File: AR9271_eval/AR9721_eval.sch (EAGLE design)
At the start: 125 parts, among them J1 UJ2-MIBH2-4-SMT-TR, J3 HTST-110-01-XX-DV, J7 132134-15, J8 132134-15, U1 U-ATHEROS-AR9271, U2 AT24C04C-XHM-T, U3 LT3080EQPBF, U4 LT3080EQPBF, U5 LT3080EQPBF, U6 LT3080EQPBF, Y1 ECS-400-10-36-CKY-TR

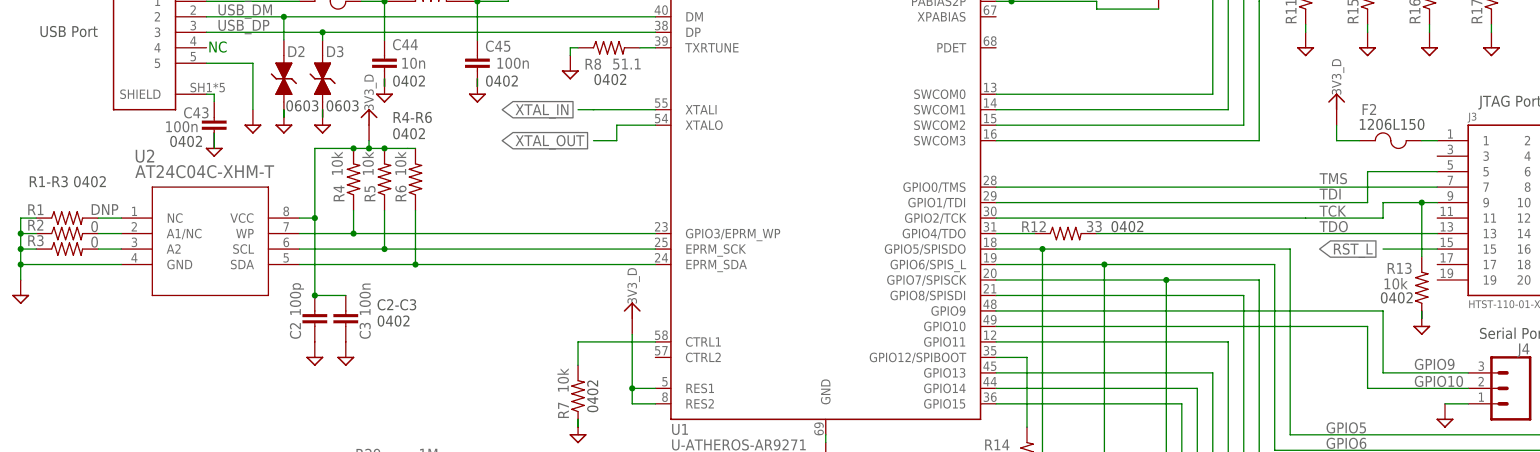
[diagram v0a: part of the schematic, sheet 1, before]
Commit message: BRD and SCH now back in sync
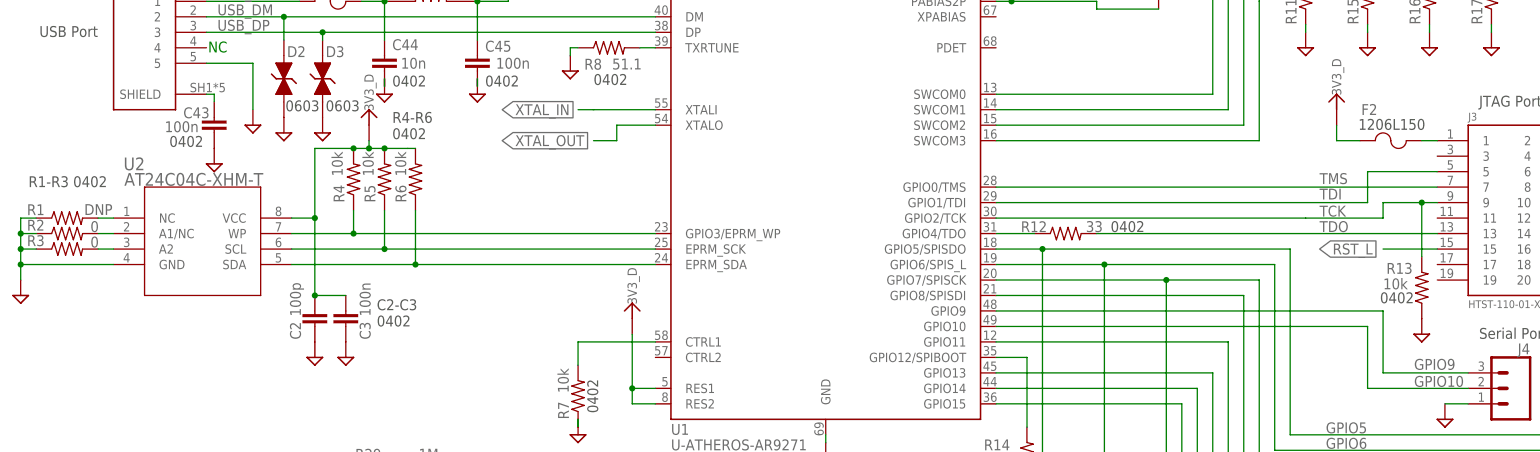
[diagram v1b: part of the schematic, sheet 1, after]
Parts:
- U2: device AT24C04_TSSOP:AT24C04C-XHM-T -> U-Generic-AT24C04-EEPROM-I2C-4Kb-TSSOP:AT24C04C-XHM-T; MPN AT24C04CXHMT -> (none)
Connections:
- removed net GND1: C43.2, D2.2, D3.2, J1.5, J2.1, J2.2, J2.7, J2.8, J3.10, J3.12, J3.14, J3.16, J3.18, J3.20, J3.4, J3.6, J3.8, J4.1, J5.1, J6.1, R1.1, R13.1, R14.1, R2.1, R3.1, U1.GND, U2.GND
- net GND: now also C43.2, D2.2, D3.2, J1.5, J2.1, J2.2, J2.7, J2.8, J3.10, J3.12, J3.14, J3.16, J3.18, J3.20, J3.4, J3.6, J3.8, J4.1, J5.1, J6.1, R1.1, R13.1, R14.1, R2.1, R3.1, U1.GND, U2.GND
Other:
- moved on the sheet: U2

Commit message: First pass of the updated AR9271 dev board. Took Stephen's fine board, and OCD'd it. Still requires stiching, better LAYER3 power layout, TNAMES cleanup, better stiching, but it's close!
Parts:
- removed F1, F2: 1206L150THWR, Polyfuse_1206L150:1206L150THWR
- removed J2: (no value), SparkFun-Connectors:CONN_08LONGPADS
- removed J4: (no value), SparkFun-Connectors:CONN_03LONGPADS
- removed J5: (no value), SparkFun-Connectors:CONN_05
- removed J6: (no value), SparkFun-Connectors:CONN_09LONGPADS
- added C52: 1u, oresat-rcl:C-EU0402-B-NOSILK
- added JP1: (no value), pinhead:PINHD-1X5
- added JP2: (no value), pinhead:PINHD-1X3
- added JP3: (no value), pinhead:PINHD-1X9
- added JP4: (no value), pinhead:PINHD-1X8
- added TP1, TP2, TP3, TP4, TP5: TPTP06R, testpad:TPTP06R
- C2: value 100p -> 100n; MPN GCM1555C1H101JA16D -> GRM155R70J105KA12J
- C35, C36: value 10.0pF -> 10p
- C37: value 100pF -> 100p
- C38, C40: value 1000pF -> 1n
- C39: value 10nF -> 10n
- C41, C42: value 1uF -> 1u
- R5, R6: value 10k -> 4.7k
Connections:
- net N$11 renamed BIASREF
- net N$16 renamed TDO-PRE-RES
- net N$2 renamed TXRTUNE
- net N$3 renamed EE-WP
- net N$4 renamed EE-SCK
- net N$5 renamed EE-SDA
- net N$8 renamed A1
- net N$9 renamed A2
- net RST_L renamed !RST
- net XTAL_IN renamed XTALI
- net XTAL_OUT renamed XTALO
- removed net N$1: R7.2, U1.CTRL1
- removed net N$10: R14.2, U1.GPIO12/SPIBOOT
- removed net N$31: C44.1, F1.2, L5.1
- removed net N$32: F2.2, J3.1
- new net CTRL1: R7.2, TP1.TP, U1.CTRL1
- new net CTRL2: TP2.TP, U1.CTRL2
- new net PDET: TP4.TP, U1.PDET
- new net SPIBOOT: R14.2, TP5.TP, U1.GPIO12/SPIBOOT
- new net XPABIOS: TP3.TP, U1.XPABIAS
- net 1V2_A: now also C2.1
- net 3V3_A: now also C52.1
- net 3V3_D: now also J3.1; no longer C2.1, F2.1
- net GND: now also C52.2, JP1.5, JP2.3, JP3.9, JP4.1, JP4.2, JP4.7, JP4.8; no longer J2.1, J2.2, J2.7, J2.8, J4.1, J5.1, J6.1
- net GPIO10: now also JP2.2; no longer J4.2
- net GPIO11: now also JP3.5; no longer J6.5
- net GPIO13: now also JP3.6; no longer J6.4
- net GPIO14: now also JP3.7; no longer J6.3
- net GPIO15: now also JP3.8; no longer J6.2
- net GPIO5: now also JP3.1; no longer J6.9
- net GPIO6: now also JP3.2; no longer J6.8
- net GPIO7: now also JP3.3; no longer J6.7
- net GPIO8: now also JP3.4; no longer J6.6
- net GPIO9: now also JP2.1; no longer J4.3
- net LDO_IN: now also JP4.5; no longer J2.4
- net N$6: now also JP4.3, JP4.4; no longer J2.5, J2.6
- net SWCOM0: now also JP1.1; no longer J5.5
- net SWCOM1: now also JP1.2; no longer J5.4
- net SWCOM2: now also JP1.3; no longer J5.3
- net SWCOM3: now also JP1.4; no longer J5.2
- net USB+5V: now also JP4.6; no longer J2.3
- net USB_+V: now also C44.1, L5.1; no longer F1.1
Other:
- note added: "40 MHz"
- note added: "DC Power Select"
- note added: "To RF feed"
- note added: "by 53"
- note added: "by p 56, 59,61"
- note removed: "0402"
- note removed: "1206L150"
- note removed: "All LEDs 0603 All dropping resistors 0402 All dropping resistors 510 Ohms for ~2.5mA LED current"
- note removed: "C2-C3 0402"
- note removed: "C4-C5 0402"
- note removed: "DC Power"
- note removed: "R1-R3 0402"
- note removed: "R4-R6 0402"
- note removed: "by p 59,61"
- moved on the sheet: C24, C25, C26, C27, C28, C29, C3, C30, C31, C32, C33, C34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

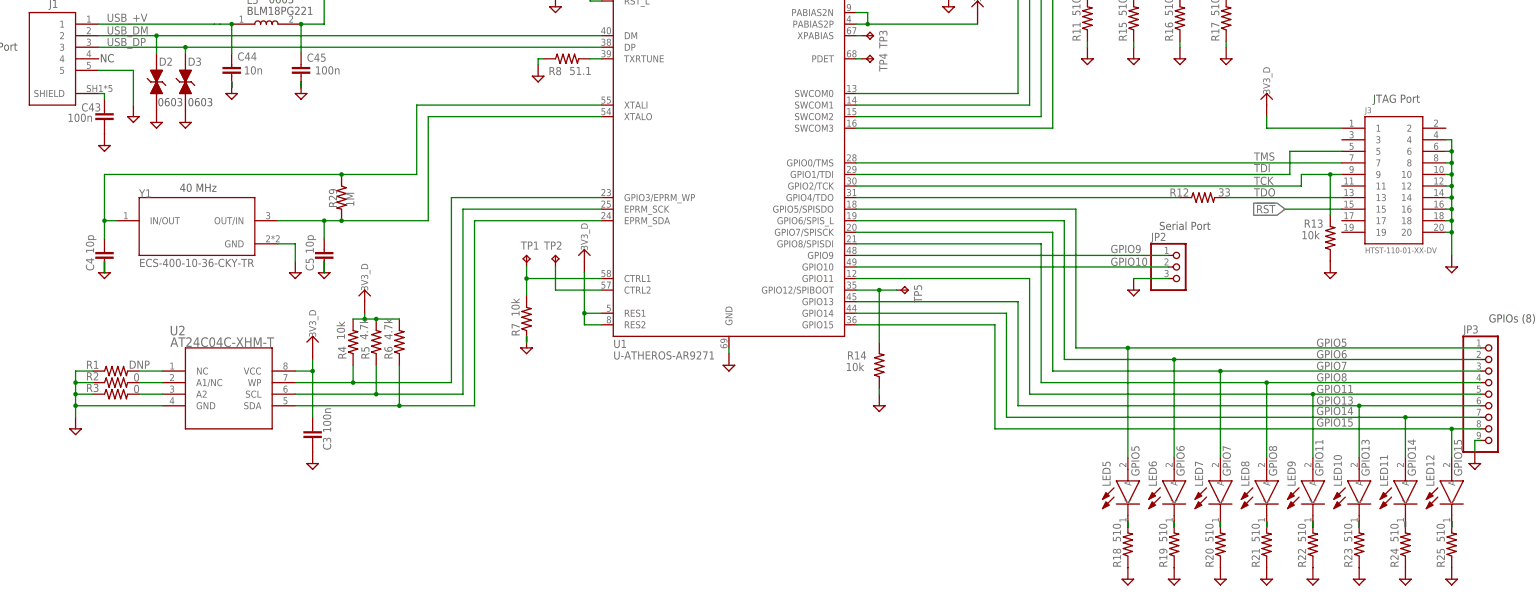
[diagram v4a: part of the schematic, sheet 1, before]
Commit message: More stitching, polishing of power layer, no ERCs or DRCs.
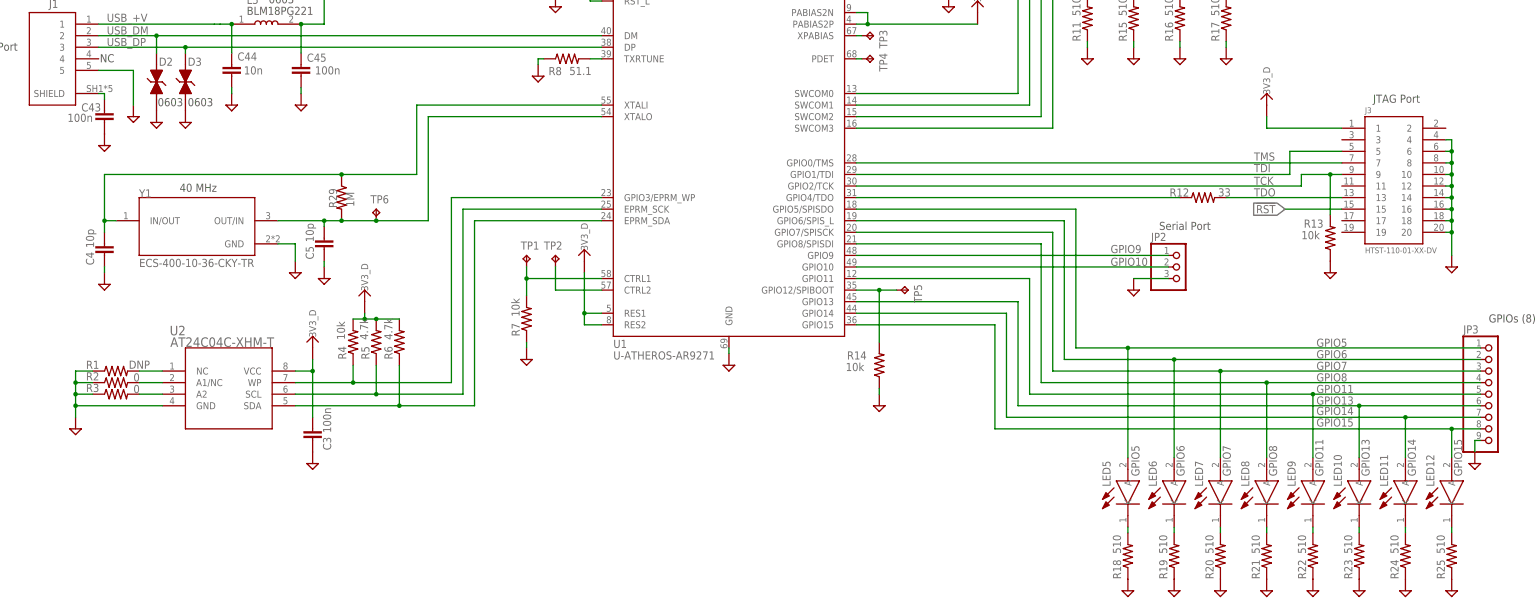
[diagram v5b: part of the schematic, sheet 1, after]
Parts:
- added C53: 4.7uF, rcl:C-EUC1206
- added TP6: TPTP06R, testpad:TPTP06R
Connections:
- net 3V3_D: now also C53.1
- net GND: now also C53.2
- net XTALO: now also TP6.TP
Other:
- note added: "Charge Resevoir"
- moved on the sheet: C4, C5, L1, R18, R19, R20, R21, R22, R23, R24, R25

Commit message: Final polish.
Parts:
- removed TP1: TPTP06R, testpad:TPTP06R
- added TP7: TPTP06R, testpad:TPTP06R
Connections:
- new net N$1: J1.4, TP7.TP
- net CTRL1: no longer TP1.TP
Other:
- note removed: "NC"
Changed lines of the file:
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@@
 <setting verticaltext="up"/>
 </settings>
-<grid distance="0.05" unitdist="inch" unit="inch" style="lines" multiple="2" display="no" altdistance="0.01" altunitdist="inch" altunit="inch"/>
+<grid distance="0.1" unitdist="inch" unit="inch" style="lines" multiple="1" display="no" altdistance="0.01" altunitdist="inch" altunit="inch"/>
 <layers>
 <layer number="1" name="Top" color="4" fill="1" visible="no" active="no"/>
@@
 <part name="FRAME4" library="frames" library_urn="urn:adsk.eagle:library:229" deviceset="FRAME_B_L" device=""/>
 <part name="U$14" library="3V3_D" deviceset="3V3_D" device=""/>
-<part name="TP1" library="testpad" library_urn="urn:adsk.eagle:library:385" deviceset="TP" device="TP06R" package3d_urn="urn:adsk.eagle:package:27954/1" value="TPTP06R"/>
 <part name="TP2" library="testpad" library_urn="urn:adsk.eagle:library:385" deviceset="TP" device="TP06R" package3d_urn="urn:adsk.eagle:package:27954/1" value="TPTP06R"/>
 <part name="C2" library="oresat-rcl" deviceset="C-EU" device="0402-B-NOSILK" value="100n">
@@
 <part name="SUPPLY80" library="supply2" library_urn="urn:adsk.eagle:library:372" deviceset="GND" device=""/>
 <part name="U$15" library="3V3_D" deviceset="3V3_D" device=""/>
+<part name="TP7" library="testpad" library_urn="urn:adsk.eagle:library:385" deviceset="TP" device="TP06R" package3d_urn="urn:adsk.eagle:package:27954/1" value="TPTP06R"/>
 </parts>
 <sheets>
@@
 <text x="86.106" y="216.408" size="1.778" layer="97">Ground</text>
 <text x="82.296" y="213.868" size="1.778" layer="97">Lab Supply</text>
-<text x="70.104" y="169.418" size="1.778" layer="97">NC</text>
 <text x="44.45" y="214.63" size="1.27" layer="97">To use USB for LDO input, connect
 connect Pin 3 to Pin 4 with jumper clip.</text>
@@
 </instance>
 <instance part="U$14" gate="G$1" x="116.84" y="109.22" smashed="yes"/>
-<instance part="TP1" gate="G$1" x="163.83" y="127" smashed="yes">
-<attribute name="NAME" x="162.56" y="128.27" size="1.778" layer="95"/>
-<attribute name="TP_SIGNAL_NAME" x="165.1" y="125.73" size="1.778" layer="97"/>
-</instance>
 <instance part="TP2" gate="G$1" x="170.18" y="127" smashed="yes">
 <attribute name="NAME" x="167.64" y="128.27" size="1.778" layer="95"/>
@@
 <attribute name="NAME" x="129.54" y="138.43" size="1.778" layer="95"/>
 <attribute name="TP_SIGNAL_NAME" x="132.08" y="135.89" size="1.778" layer="97"/>
+</instance>
+<instance part="TP7" gate="G$1" x="77.47" y="185.42" smashed="yes">
+<attribute name="NAME" x="76.2" y="186.69" size="1.778" layer="95"/>
+<attribute name="TP_SIGNAL_NAME" x="78.74" y="184.15" size="1.778" layer="97"/>
 </instance>
 </instances>
@@
 <pinref part="U1" gate="G$1" pin="CTRL1"/>
 <pinref part="R7" gate="R" pin="2"/>
-<wire x1="163.83" y1="124.46" x2="163.83" y2="121.92" width="0.1524" layer="91"/>
-<pinref part="TP1" gate="G$1" pin="TP"/>
 <wire x1="163.83" y1="121.92" x2="163.83" y2="118.11" width="0.1524" layer="91"/>
 <wire x1="180.34" y1="121.92" x2="163.83" y2="121.92" width="0.1524" layer="91"/>
-<junction x="163.83" y="121.92"/>
 </segment>
 </net>
@@
 </segment>
 </net>
+<net name="N$1" class="0">
+<segment>
+<pinref part="J1" gate="G$1" pin="4"/>
+<pinref part="TP7" gate="G$1" pin="TP"/>
+<wire x1="69.85" y1="170.18" x2="77.47" y2="170.18" width="0.1524" layer="91"/>
+<wire x1="77.47" y1="170.18" x2="77.47" y2="182.88" width="0.1524" layer="91"/>
+</segment>
+</net>

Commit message: Added holes for feet, more stitching, and DRC cleanup. DONE! SHIP IT!
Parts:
- added H1, H2, H3, H4: STAND-OFFTIGHT, SparkFun-Hardware:STAND-OFFTIGHT
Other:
- note added: "Standoffs"
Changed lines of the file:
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@@
 <setting verticaltext="up"/>
 </settings>
-<grid distance="0.1" unitdist="inch" unit="inch" style="lines" multiple="1" display="no" altdistance="0.01" altunitdist="inch" altunit="inch"/>
+<grid distance="0.05" unitdist="inch" unit="inch" style="lines" multiple="2" display="no" altdistance="0.01" altunitdist="inch" altunit="inch"/>
 <layers>
 <layer number="1" name="Top" color="4" fill="1" visible="no" active="no"/>
@@
 <layer number="99" name="SpiceOrder" color="7" fill="1" visible="yes" active="yes"/>
 <layer number="100" name="Muster" color="7" fill="1" visible="no" active="no"/>
+<layer number="101" name="Patch_Top" color="12" fill="4" visible="yes" active="yes"/>
+<layer number="102" name="Vscore" color="7" fill="1" visible="yes" active="yes"/>
+<layer number="103" name="tMap" color="7" fill="1" visible="yes" active="yes"/>
+<layer number="104" name="Name" color="16" fill="1" visible="yes" active="yes"/>
+<layer number="105" name="tPlate" color="7" fill="1" visible="yes" active="yes"/>
+<layer number="106" name="bPlate" color="7" fill="1" visible="yes" active="yes"/>
+<layer number="107" name="Crop" color="7" fill="1" visible="yes" active="yes"/>
+<layer number="108" name="tplace-old" color="10" fill="1" visible="yes" active="yes"/>
+<layer number="109" name="ref-old" color="11" fill="1" visible="yes" active="yes"/>
+<layer number="110" name="fp0" color="7" fill="1" visible="yes" active="yes"/>
+<layer number="111" name="LPC17xx" color="7" fill="1" visible="yes" active="yes"/>
+<layer number="112" name="tSilk" color="7" fill="1" visible="yes" active="yes"/>
+<layer number="113" name="IDFDebug" color="4" fill="1" visible="yes" active="yes"/>
+<layer number="114" name="Badge_Outline" color="7" fill="1" visible="yes" active="yes"/>
+<layer number="116" name="Patch_BOT" color="9" fill="4" visible="yes" active="yes"/>
+<layer number="118" name="Rect_Pads" color="7" fill="1" visible="yes" active="yes"/>
+<layer number="121" name="_tsilk" color="7" fill="1" visible="yes" active="yes"/>
+<layer number="122" name="_bsilk" color="7" fill="1" visible="yes" active="yes"/>
+<layer number="123" name="tTestmark" color="7" fill="1" visible="yes" active="yes"/>
+<layer number="124" name="bTestmark" color="7" fill="1" visible="yes" active="yes"/>
+<layer number="125" name="_tNames" color="7" fill="1" visible="yes" active="yes"/>
+<layer number="126" name="_bNames" color="7" fill="1" visible="yes" active="yes"/>
+<layer number="127" name="_tValues" color="7" fill="1" visible="yes" active="yes"/>
+<layer number="128" name="_bValues" color="7" fill="1" visible="yes" active="yes"/>
+<layer number="129" name="Mask" color="7" fill="1" visible="yes" active="yes"/>
+<layer number="131" name="tAdjust" color="7" fill="1" visible="yes" active="yes"/>
+<layer number="132" name="bAdjust" color="7" fill="1" visible="yes" active="yes"/>
+<layer number="144" name="Drill_legend" color="7" fill="1" visible="yes" active="yes"/>
+<layer number="150" name="Notes" color="7" fill="1" visible="yes" active="yes"/>
+<layer number="151" name="HeatSink" color="7" fill="1" visible="yes" active="yes"/>
+<layer number="152" name="_bDocu" color="7" fill="1" visible="yes" active="yes"/>
+<layer number="153" name="FabDoc1" color="7" fill="1" visible="yes" active="yes"/>
+<layer number="154" name="FabDoc2" color="7" fill="1" visible="yes" active="yes"/>
+<layer number="155" name="FabDoc3" color="7" fill="1" visible="yes" active="yes"/>
+<layer number="199" name="Contour" color="7" fill="1" visible="yes" active="yes"/>
+<layer number="200" name="200bmp" color="1" fill="10" visible="yes" active="yes"/>
+<layer number="201" name="201bmp" color="2" fill="10" visible="yes" active="yes"/>
+<layer number="202" name="202bmp" color="3" fill="10" visible="yes" active="yes"/>
+<layer number="203" name="203bmp" color="4" fill="10" visible="yes" active="yes"/>
+<layer number="204" name="204bmp" color="5" fill="10" visible="yes" active="yes"/>
+<layer number="205" name="205bmp" color="6" fill="10" visible="yes" active="yes"/>
+<layer number="206" name="206bmp" color="7" fill="10" visible="yes" active="yes"/>
+<layer number="207" name="207bmp" color="8" fill="10" visible="yes" active="yes"/>
+<layer number="208" name="208bmp" color="9" fill="10" visible="yes" active="yes"/>
+<layer number="209" name="209bmp" color="7" fill="1" visible="yes" active="yes"/>
+<layer number="210" name="210bmp" color="7" fill="1" visible="yes" active="yes"/>
+<layer number="211" name="211bmp" color="7" fill="1" visible="yes" active="yes"/>
+<layer number="212" name="212bmp" color="7" fill="1" visible="yes" active="yes"/>
+<layer number="213" name="213bmp" color="7" fill="1" visible="yes" active="yes"/>
+<layer number="214" name="214bmp" color="7" fill="1" visible="yes" active="yes"/>
+<layer number="215" name="215bmp" color="7" fill="1" visible="yes" active="yes"/>
+<layer number="216" name="216bmp" color="7" fill="1" visible="yes" active="yes"/>
 <layer number="217" name="217bmp" color="18" fill="1" visible="no" active="no"/>
 <layer number="218" name="218bmp" color="19" fill="1" visible="no" active="no"/>
@@
 <layer number="223" name="223bmp" color="24" fill="1" visible="no" active="no"/>
 <layer number="224" name="224bmp" color="25" fill="1" visible="no" active="no"/>
+<layer number="225" name="225bmp" color="7" fill="1" visible="yes" active="yes"/>
+<layer number="226" name="226bmp" color="7" fill="1" visible="yes" active="yes"/>
+<layer number="227" name="227bmp" color="7" fill="1" visible="yes" active="yes"/>
+<layer number="228" name="228bmp" color="7" fill="1" visible="yes" active="yes"/>
+<layer number="229" name="229bmp" color="7" fill="1" visible="yes" active="yes"/>
+<layer number="230" name="230bmp" color="7" fill="1" visible="yes" active="yes"/>
+<layer number="231" name="231bmp" color="7" fill="1" visible="yes" active="yes"/>
+<layer number="248" name="Housing" color="7" fill="1" visible="yes" active="yes"/>
+<layer number="249" name="Edge" color="7" fill="1" visible="yes" active="yes"/>
 <layer number="250" name="Descript" color="3" fill="1" visible="no" active="no"/>
 <layer number="251" name="SMDround" color="12" fill="11" visible="no" active="no"/>
+<layer number="254" name="cooling" color="7" fill="1" visible="yes" active="yes"/>
+<layer number="255" name="routoute" color="7" fill="1" visible="yes" active="yes"/>
 </layers>
 <schematic xreflabel="%F%N/%S.%C%R" xrefpart="/%S.%C%R">
@@
 <part name="U$15" library="3V3_D" deviceset="3V3_D" device=""/>
 <part name="TP7" library="testpad" library_urn="urn:adsk.eagle:library:385" deviceset="TP" device="TP06R" package3d_urn="urn:adsk.eagle:package:27954/1" value="TPTP06R"/>
+<part name="H1" library="SparkFun-Hardware" library_urn="urn:adsk.eagle:library:519" deviceset="STAND-OFF" device="TIGHT" package3d_urn="urn:adsk.eagle:package:38629/1"/>
+<part name="H2" library="SparkFun-Hardware" library_urn="urn:adsk.eagle:library:519" deviceset="STAND-OFF" device="TIGHT" package3d_urn="urn:adsk.eagle:package:38629/1"/>
+<part name="H3" library="SparkFun-Hardware" library_urn="urn:adsk.eagle:library:519" deviceset="STAND-OFF" device="TIGHT" package3d_urn="urn:adsk.eagle:package:38629/1"/>
+<part name="H4" library="SparkFun-Hardware" library_urn="urn:adsk.eagle:library:519" deviceset="STAND-OFF" device="TIGHT" package3d_urn="urn:adsk.eagle:package:38629/1"/>
 </parts>
 <sheets>
@@
 <wire x1="307.34" y1="228.6" x2="304.8" y2="228.6" width="0.1524" layer="97"/>
 <text x="309.88" y="240.03" size="1.778" layer="97" rot="R90">To RF feed</text>
+<text x="265.43" y="6.35" size="1.778" layer="97">Standoffs</text>
 </plain>
 <instances>
@@
 <attribute name="TP_SIGNAL_NAME" x="78.74" y="184.15" size="1.778" layer="97"/>
 </instance>
+<instance part="H1" gate="G$1" x="266.7" y="2.54" smashed="yes"/>
+<instance part="H2" gate="G$1" x="269.24" y="2.54" smashed="yes"/>
+<instance part="H3" gate="G$1" x="271.78" y="2.54" smashed="yes"/>
+<instance part="H4" gate="G$1" x="274.32" y="2.54" smashed="yes"/>
 </instances>
 <busses>
